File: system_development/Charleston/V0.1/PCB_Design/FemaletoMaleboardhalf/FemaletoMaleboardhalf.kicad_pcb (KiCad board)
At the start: 2 copper layers, 34.8 x 64.4 mm, 2 parts, among them J1 Screw_Terminal_01x12

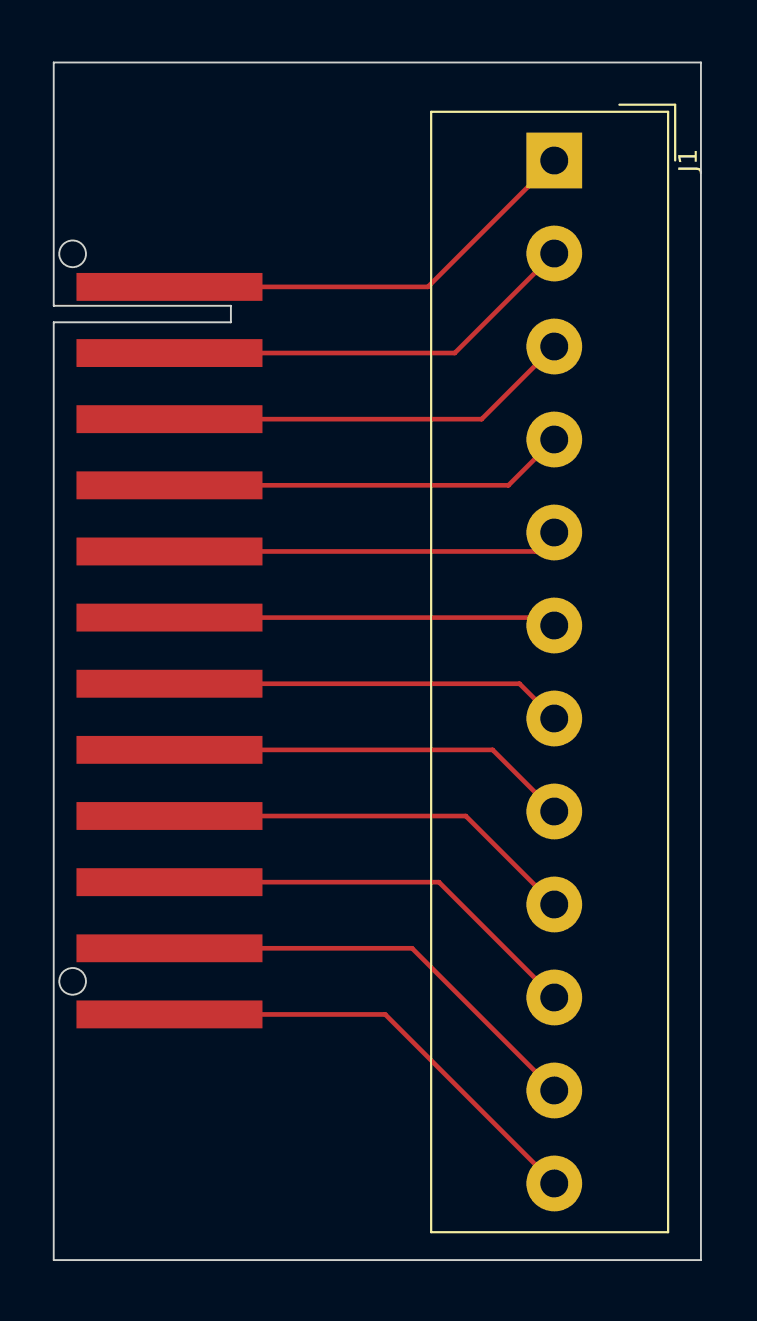
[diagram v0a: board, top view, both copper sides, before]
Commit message: V0.1
Added ground plane, standoff holes, USC/ARTS lab logo, name, date, and version
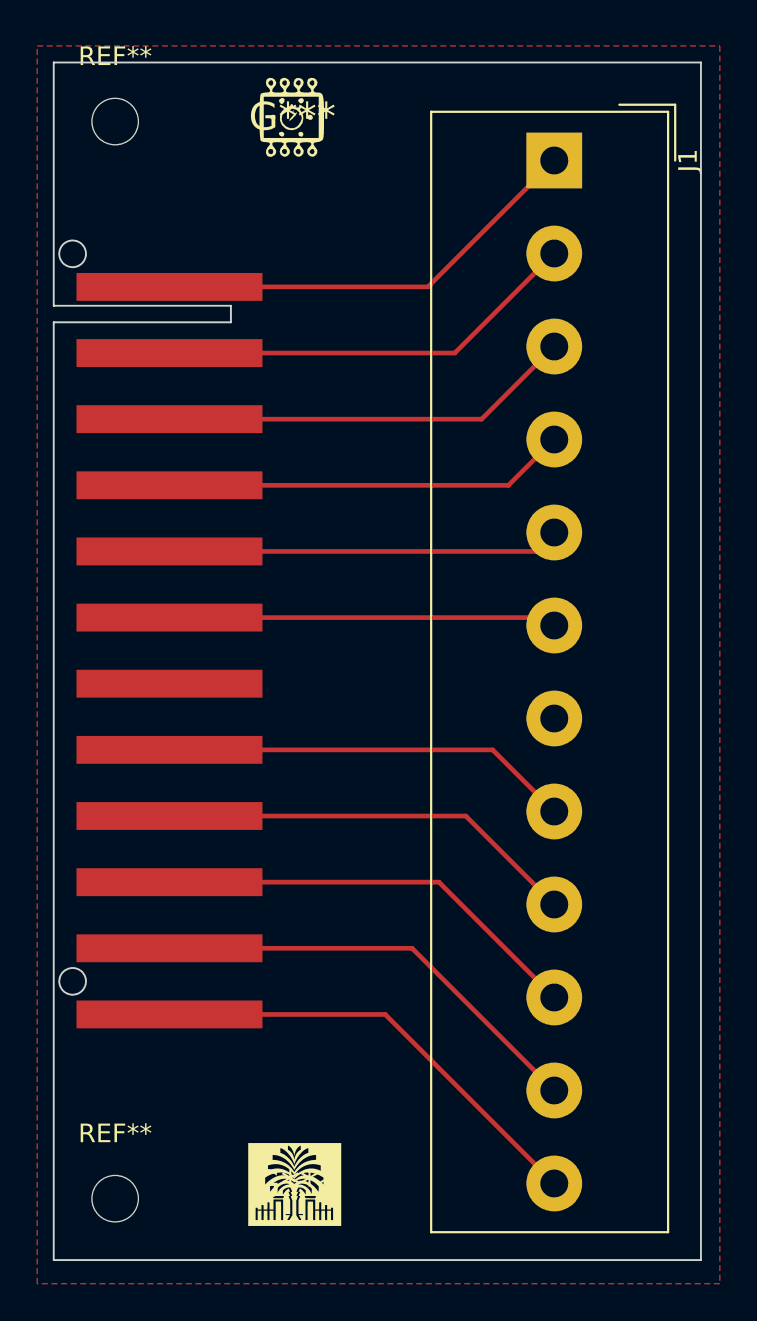
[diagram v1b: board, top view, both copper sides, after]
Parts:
- added G***: LOGO, BMS_PCB_Library:ARTSLABLOGO, F.Cu at (122.7, 64.0)
- added G***: LOGO, BMS_PCB_Library:USCLOGO, F.Cu at (122.8, 121.4)
- added REF**: MountingHole_2.5mm, MountingHole:MountingHole_2.5mm, F.Cu at (113.2, 122.2)
- added REF**: MountingHole_2.5mm, MountingHole:MountingHole_2.5mm, F.Cu at (113.2, 64.3)
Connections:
- net Net-(J1-Pin_7) renamed GND
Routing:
- net GND: track 21.5 -> 0.00 mm
- added copper zone on F.Cu, net GND

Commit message: Propper text and logo
Proper text and logo
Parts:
- removed the G*** at (122.7, 64.0)
- added G***: LOGO, BMS_PCB_Library:ARTSLAB, F.Cu at (124.0, 122.9)
- moved G*** 58.0 mm to (123.8, 63.4)
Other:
- board text added: "6/6/24"
- board text added: "Parker Jackson"
- board text added: "V0.1"
